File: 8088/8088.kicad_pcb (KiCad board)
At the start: 2 copper layers, 157.5 x 93.5 mm, 194 parts, among them P10 CONN_01X15, P11 CONN_01X05, P12 CONN_01X05, P13 CONN_01X08, P14 CONN_01X08, P9 CONN_01X06, U1 8284, U10 2114, U11 ULN2803ADWR, U12 74LS14, U13 ULN2803ADWR, U14 ULN2803ADWR, U15 ULN2803ADWR, U16 LM1084IT-5.0/NOPB, U2 8088, U3 8755A, U3PA U3PA, U3PB U3PB, U4 8155, U4PA U4PA, U4PB U4PB, U4PC U4PC, U5 8251A, U6 74LS32, U7 74LS138, U8 8282, U9 2114, Y1 12MHz

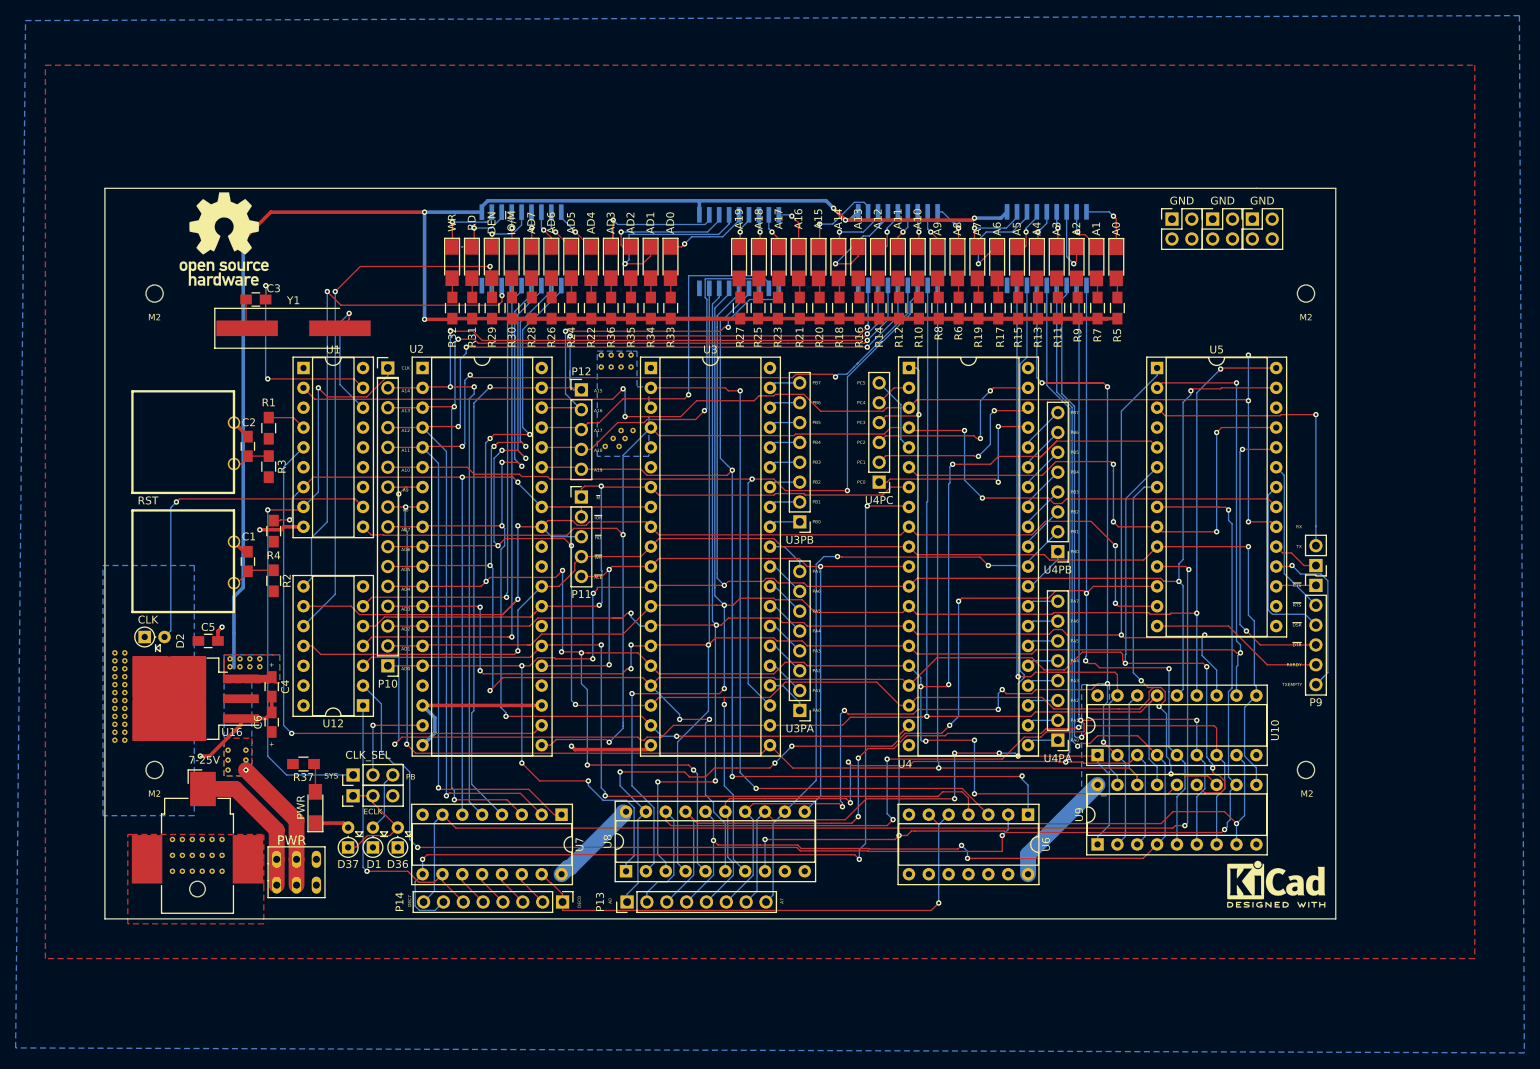
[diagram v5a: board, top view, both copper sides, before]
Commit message: Board rev2 done. Added buck converter circuit
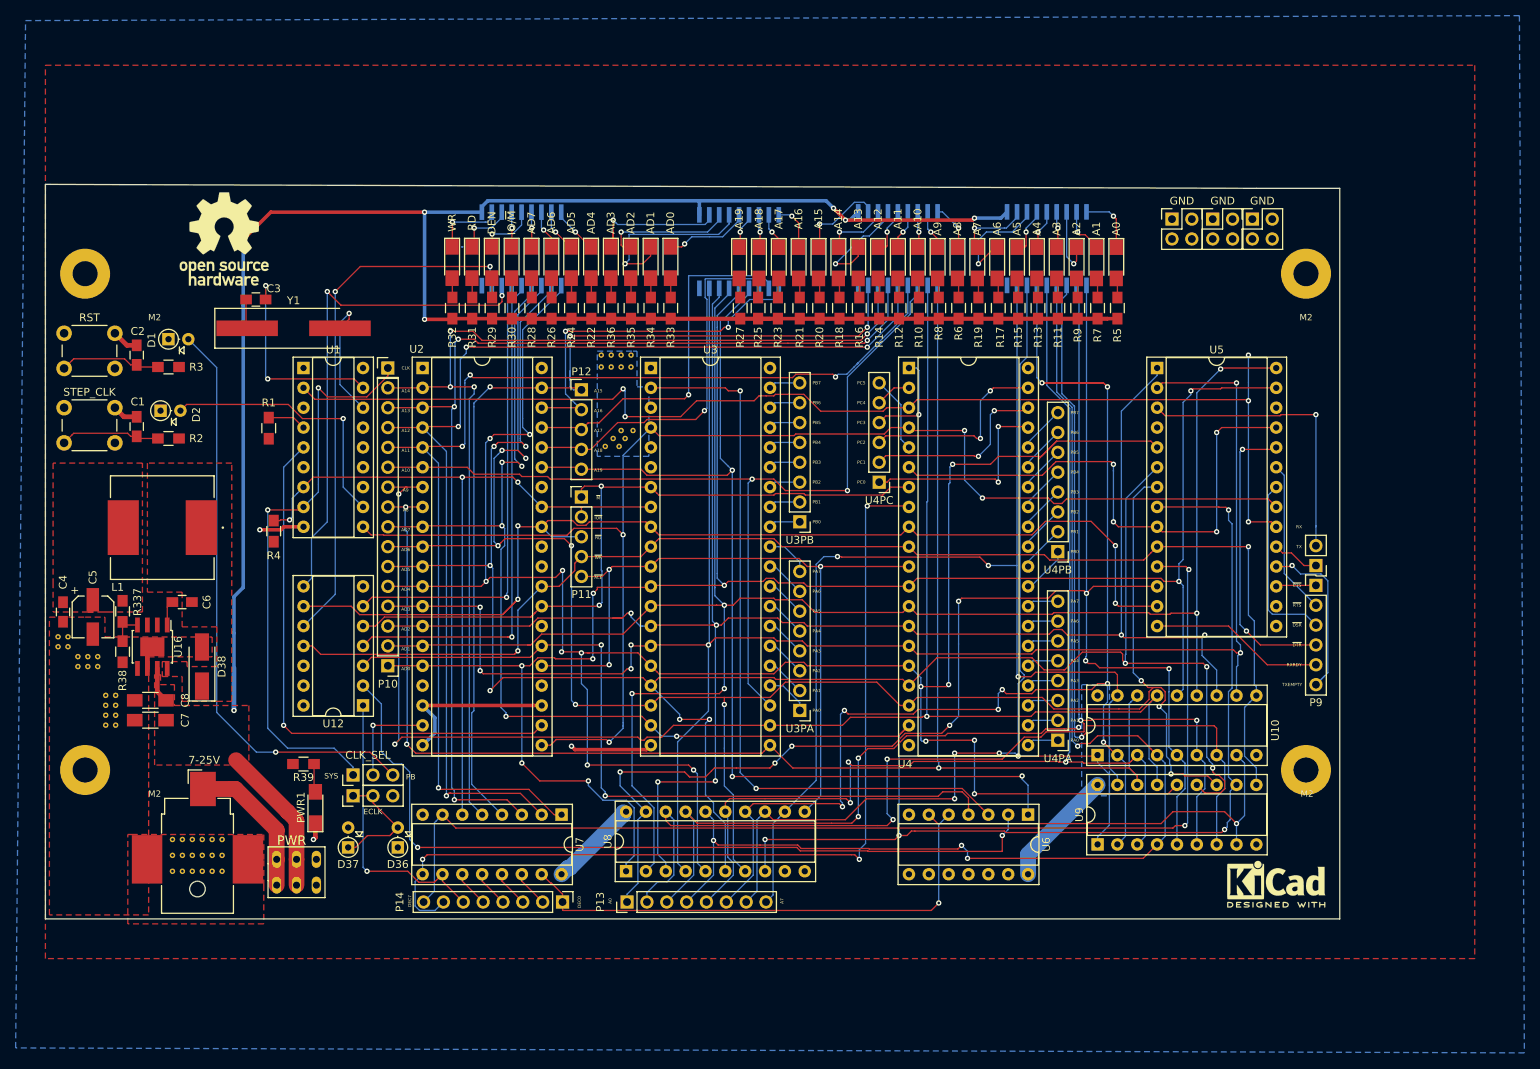
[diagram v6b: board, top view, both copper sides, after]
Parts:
- removed the CLK at (85.1, 88.9)
- removed the REF** at (76.2, 111.8)
- removed the REF** at (76.2, 102.6)
- removed the REF** at (76.2, 101.6)
- removed the REF** at (76.2, 100.6)
- removed the REF** at (74.9, 100.6)
- removed the REF** at (74.9, 101.6)
- removed the REF** at (74.9, 102.6)
- removed the REF** at (74.9, 103.6)
- removed the REF** at (74.9, 104.6)
- removed the REF** at (74.9, 105.7)
- removed the REF** at (74.9, 106.7)
- removed the REF** at (76.2, 110.7)
- removed the REF** at (74.9, 107.7)
- removed the REF** at (74.9, 108.7)
- removed the REF** at (74.9, 109.7)
- removed the REF** at (74.9, 110.7)
- removed the REF** at (74.9, 111.8)
- removed the REF** at (93.5, 102.4)
- removed the REF** at (92.2, 102.4)
- removed the REF** at (90.9, 102.4)
- removed the REF** at (89.7, 102.4)
- removed the REF** at (89.7, 101.3)
- removed the REF** at (76.2, 109.7)
- removed the REF** at (90.9, 101.3)
- removed the REF** at (92.2, 101.3)
- removed the REF** at (93.5, 101.3)
- removed the REF** at (89.4, 113.0)
- removed the REF** at (91.7, 113.0)
- removed the REF** at (91.7, 114.3)
- removed the REF** at (89.4, 114.3)
- removed the REF** at (89.4, 115.6)
- removed the REF** at (76.2, 108.7)
- removed the REF** at (76.2, 107.7)
- removed the REF** at (76.2, 106.7)
- removed the REF** at (80.0, 54.6)
- removed the REF** at (76.2, 105.7)
- removed the REF** at (227.3, 54.6)
- removed the REF** at (227.3, 115.6)
- removed the REF** at (80.0, 115.6)
- removed the REF** at (76.2, 104.6)
- removed the REF** at (76.2, 103.6)
- removed the RST at (85.1, 73.7)
- added C7: 4.7uF, Capacitors_SMD:C_1206_HandSoldering, F.Cu at (79.5, 109.2)
- added C8: 4.7uF, Capacitors_SMD:C_1206_HandSoldering, F.Cu at (79.5, 106.7)
- added D38: STPS5L60U, Diodes_SMD:D_SMA_Handsoldering, F.Cu at (86.1, 102.3)
- added L1: 22uH, footprints:SRR1208-220ML, F.Cu at (81.0, 84.6)
- added R337: 30.9K±0.1%, Resistors_SMD:R_0805_HandSoldering, F.Cu at (75.9, 95.3)
- added R38: 10K±0.1%, Resistors_SMD:R_0805_HandSoldering, F.Cu at (75.9, 100.4)
- added REF**: MountingHole_3.2mm_M3_Pad, Mounting_Holes:MountingHole_3.2mm_M3_Pad, F.Cu at (71.1, 52.1)
- added REF**: MountingHole_3.2mm_M3_Pad, Mounting_Holes:MountingHole_3.2mm_M3_Pad, F.Cu at (71.1, 115.6)
- added REF**: MountingHole_3.2mm_M3_Pad, Mounting_Holes:MountingHole_3.2mm_M3_Pad, F.Cu at (227.3, 115.6)
- added REF**: via-0.7mm, footprints:via-0.7mm, F.Cu at (67.7, 98.5)
- added REF**: via-0.7mm, footprints:via-0.7mm, F.Cu at (68.9, 98.5)
- added REF**: via-0.7mm, footprints:via-0.7mm, F.Cu at (70.2, 101.1)
- added REF**: via-0.7mm, footprints:via-0.7mm, F.Cu at (71.5, 101.1)
- added REF**: via-0.7mm, footprints:via-0.7mm, F.Cu at (72.7, 101.1)
- added REF**: via-0.7mm, footprints:via-0.7mm, F.Cu at (75.0, 106.0)
- added REF**: via-0.7mm, footprints:via-0.7mm, F.Cu at (75.0, 107.3)
- added REF**: via-0.7mm, footprints:via-0.7mm, F.Cu at (75.0, 108.6)
- added REF**: via-0.7mm, footprints:via-0.7mm, F.Cu at (75.0, 109.8)
- added REF**: via-0.7mm, footprints:via-0.7mm, F.Cu at (73.8, 109.8)
- added REF**: via-0.7mm, footprints:via-0.7mm, F.Cu at (73.8, 108.6)
- added REF**: via-0.7mm, footprints:via-0.7mm, F.Cu at (73.8, 107.3)
- added REF**: via-0.7mm, footprints:via-0.7mm, F.Cu at (73.8, 106.0)
- added REF**: via-0.7mm, footprints:via-0.7mm, F.Cu at (72.7, 102.3)
- added REF**: via-0.7mm, footprints:via-0.7mm, F.Cu at (71.5, 102.3)
- added REF**: via-0.7mm, footprints:via-0.7mm, F.Cu at (70.2, 102.3)
- added REF**: via-0.7mm, footprints:via-0.7mm, F.Cu at (68.9, 99.8)
- added REF**: via-0.7mm, footprints:via-0.7mm, F.Cu at (67.7, 99.8)
- added REF**: MountingHole_3.2mm_M3_Pad, Mounting_Holes:MountingHole_3.2mm_M3_Pad, F.Cu at (227.3, 52.1)
- added RST: RESET, Buttons_Switches_ThroughHole:SW_PUSH_6mm_h5mm, F.Cu at (68.4, 59.7)
- added STEP_CLK: STEP_CLK, Buttons_Switches_ThroughHole:SW_PUSH_6mm_h5mm, F.Cu at (68.4, 69.2)
- C4: value 10uF -> 100nF
- C5: value 100nF -> 220uF; footprint Capacitors_SMD:C_0805_HandSoldering -> Capacitors_SMD:CP_Elec_5x5.3
- C6: value 10uF -> 10nF
- R39: renamed from R37; value 220 -> 7.5K
- U16: value LM1084IT-5.0/NOPB -> TPS5430; footprint TO_SOT_Packages_SMD:TO-263-3_TabPin2 -> Housings_SOIC:TI_SO-PowerPAD-8
- moved D1 70.1 mm to (81.8, 60.5), turned to 0 degrees
- moved D2 29.0 mm to (80.8, 69.6)
- moved C4 28.4 mm to (68.3, 95.4)
- moved R2 22.6 mm to (81.8, 73.2), turned to 0 degrees
- moved C1 22.4 mm to (77.7, 71.6)
- moved C6 19.2 mm to (83.5, 94.1), turned to 0 degrees
- moved C2 18.4 mm to (77.7, 62.5)
- moved R3 18.1 mm to (81.8, 64.0), turned to 0 degrees
- moved C5 15.1 mm to (72.1, 96.0), turned to 270 degrees
- moved U16 8.66 mm to (79.7, 99.8), turned to 270 degrees
- renumbered PWR to PWR1
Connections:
- C4 pad 1: /P_IN -> +5V
- C6 pad 1: +5V -> Net-(C6-Pad1)
- C6 pad 2: GND -> /Buck Converter/PH
- PWR pad 2: /P_IN -> P_IN
- PWR pad 5: /P_IN -> P_IN
- R10 pad 1: /P_IN -> P_IN
- R11 pad 1: /P_IN -> P_IN
- R12 pad 1: /P_IN -> P_IN
- R13 pad 1: /P_IN -> P_IN
- R14 pad 1: /P_IN -> P_IN
- R15 pad 1: /P_IN -> P_IN
- R16 pad 1: /P_IN -> P_IN
- R17 pad 1: /P_IN -> P_IN
- R18 pad 1: /P_IN -> P_IN
- R19 pad 1: /P_IN -> P_IN
- R20 pad 1: /P_IN -> P_IN
- R21 pad 1: /P_IN -> P_IN
- R22 pad 1: /P_IN -> P_IN
- R23 pad 1: /P_IN -> P_IN
- R24 pad 1: /P_IN -> P_IN
- R25 pad 1: /P_IN -> P_IN
- R26 pad 1: /P_IN -> P_IN
- R27 pad 1: /P_IN -> P_IN
- R28 pad 1: /P_IN -> P_IN
- R29 pad 1: /P_IN -> P_IN
- R30 pad 1: /P_IN -> P_IN
- R31 pad 1: /P_IN -> P_IN
- R32 pad 1: /P_IN -> P_IN
- R33 pad 1: /P_IN -> P_IN
- R34 pad 1: /P_IN -> P_IN
- R35 pad 1: /P_IN -> P_IN
- R36 pad 1: /P_IN -> P_IN
- R5 pad 1: /P_IN -> P_IN
- R6 pad 1: /P_IN -> P_IN
- R7 pad 1: /P_IN -> P_IN
- R8 pad 1: /P_IN -> P_IN
- R9 pad 1: /P_IN -> P_IN
- U11 pad 10: /P_IN -> P_IN
- U13 pad 10: /P_IN -> P_IN
- U14 pad 10: /P_IN -> P_IN
- U15 pad 10: /P_IN -> P_IN
- U16 pad 1: GND -> Net-(C6-Pad1)
- U16 pad 2: +5V -> Net-(U16-Pad2)
- U16 pad 3: /P_IN -> Net-(U16-Pad3)
- U5 pad 15: (no net) -> Net-(U5-Pad15)
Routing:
- net P_IN: track 0.00 -> 367.4 mm, vias 0 -> 7
- net /P_IN: track 359.6 -> 0.00 mm, vias 7 -> 0
- net Net-(D1-Pad2): track 8.14 -> 75.5 mm, vias 0 -> 1
- net GND: track 64.9 -> 49.1 mm, vias 4 -> 3
- net Net-(D2-Pad2): track 42.4 -> 34.3 mm
- net Net-(C2-Pad1): track 4.94 -> 13.0 mm
- net Net-(C1-Pad1): track 5.84 -> 12.8 mm
- net Net-(R37-Pad2): track 0.00 -> 4.42 mm
- net Net-(C6-Pad1): track 0.00 -> 3.21 mm
- net Net-(JP1-Pad1): track 75.7 -> 74.2 mm
- added copper zone on F.Cu, net /Buck Converter/PH
- added copper zone on F.Cu, net P_IN
- removed copper zone on B.Cu, net /P_IN
- removed copper zone on F.Cu, net /P_IN
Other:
- board size 157.5 x 93.5 mm -> 165.6 x 94 mm
- net class GND removed
- net class PWR: trace_width 2.032 -> 0.6096
- rule pad_to_mask_clearance: 0 -> 0.2
- board text removed: "+"
